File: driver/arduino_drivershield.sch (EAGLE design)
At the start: 22 parts, among them IC1 LB1973M, IC10 LB1973M, IC11 LB1973M, IC12 74HC14D, IC2 LB1973M, IC3 74HC14D, IC4 LB1973M, IC5 LB1973M, IC6 74HC14D, IC7 LB1973M, IC8 LB1973M, IC9 74HC14D, U1 ARDUINO_SHIELDLABEL

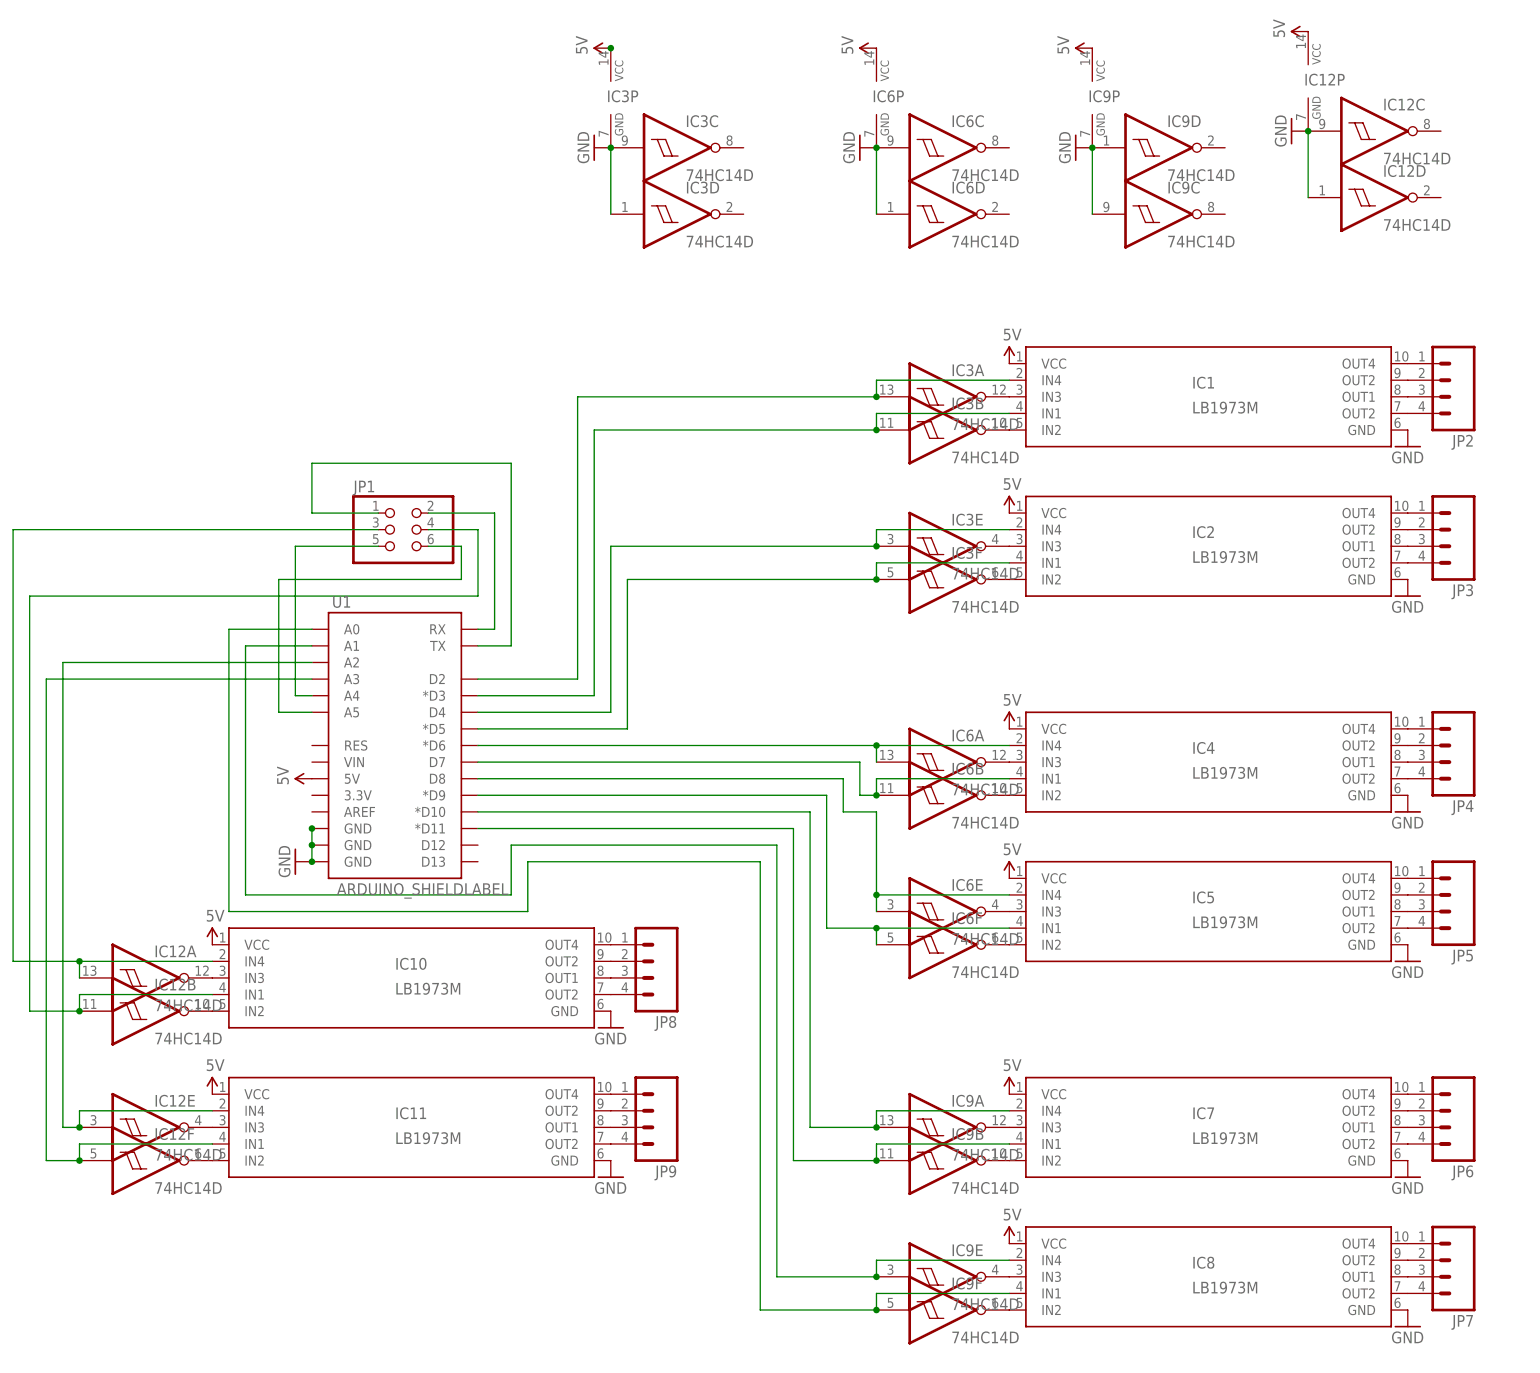
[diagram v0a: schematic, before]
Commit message: attempting to have higher power traces for the h-bridges alone (gnd is a bit tricky if I want to use the plane on the bottom for signal gnd as well
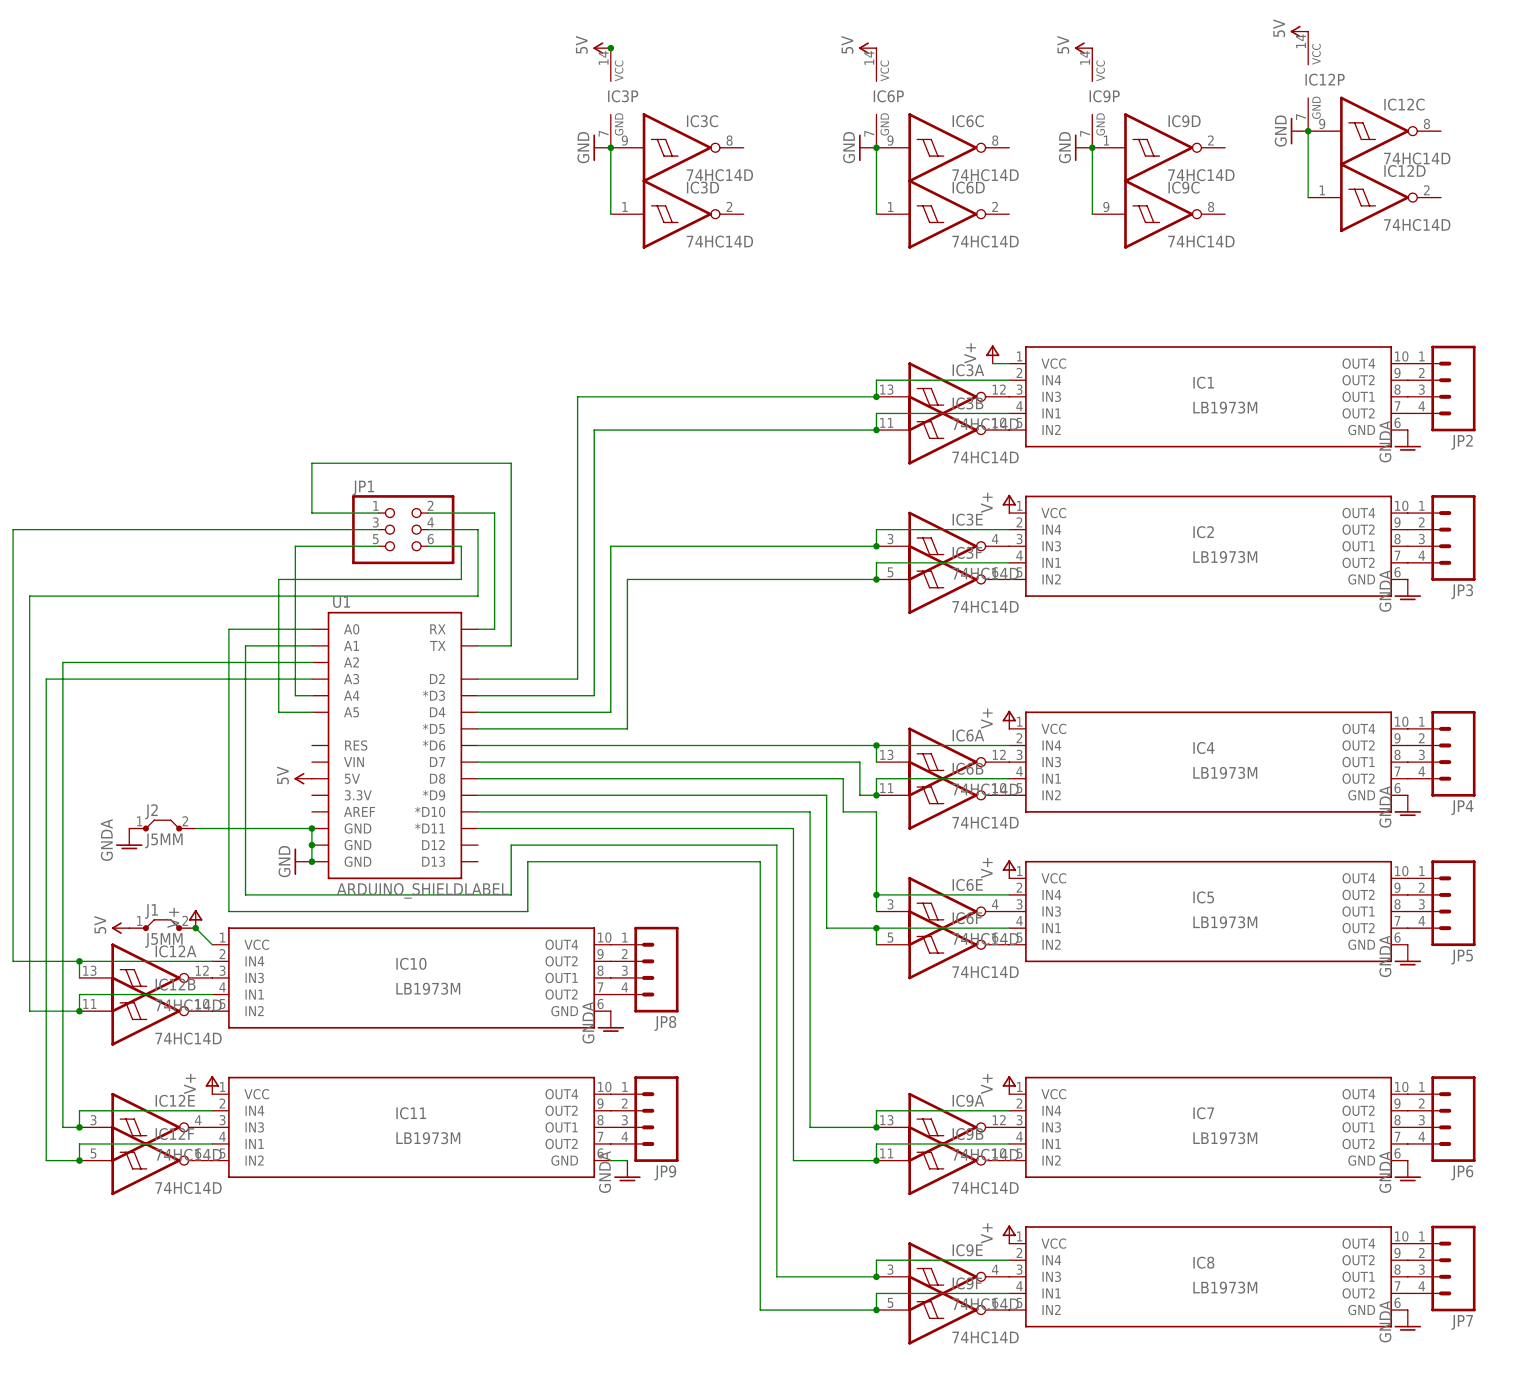
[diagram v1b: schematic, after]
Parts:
- added J1, J2: J5MM, jumper:J5MM
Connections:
- removed net GND: IC1.GND, IC10.GND, IC11.GND, IC12C.I, IC12D.I, IC12P.GND, IC2.GND, IC3C.I, IC3D.I, IC3P.GND, IC4.GND, IC5.GND, IC6C.I, IC6D.I, IC6P.GND, IC7.GND, IC8.GND, IC9C.I, IC9D.I, IC9P.GND, U1.GND@0, U1.GND@1, U1.GND@2
- new net @GND2: IC12C.I, IC12D.I, IC12P.GND, IC3C.I, IC3D.I, IC3P.GND, IC6C.I, IC6D.I, IC6P.GND, IC9C.I, IC9D.I, IC9P.GND, J2.2, U1.GND@0, U1.GND@1, U1.GND@2
- new net @GND3: IC11.GND
- new net GNDA: IC1.GND, IC10.GND, IC2.GND, IC4.GND, IC5.GND, IC7.GND, IC8.GND, J2.1
- new net V+: IC1.VCC, IC10.VCC, IC11.VCC, IC2.VCC, IC4.VCC, IC5.VCC, IC7.VCC, IC8.VCC, J1.2
- net 5V: now also J1.1; no longer IC1.VCC, IC10.VCC, IC11.VCC, IC2.VCC, IC4.VCC, IC5.VCC, IC7.VCC, IC8.VCC

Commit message: bypass caps for all h-bridges
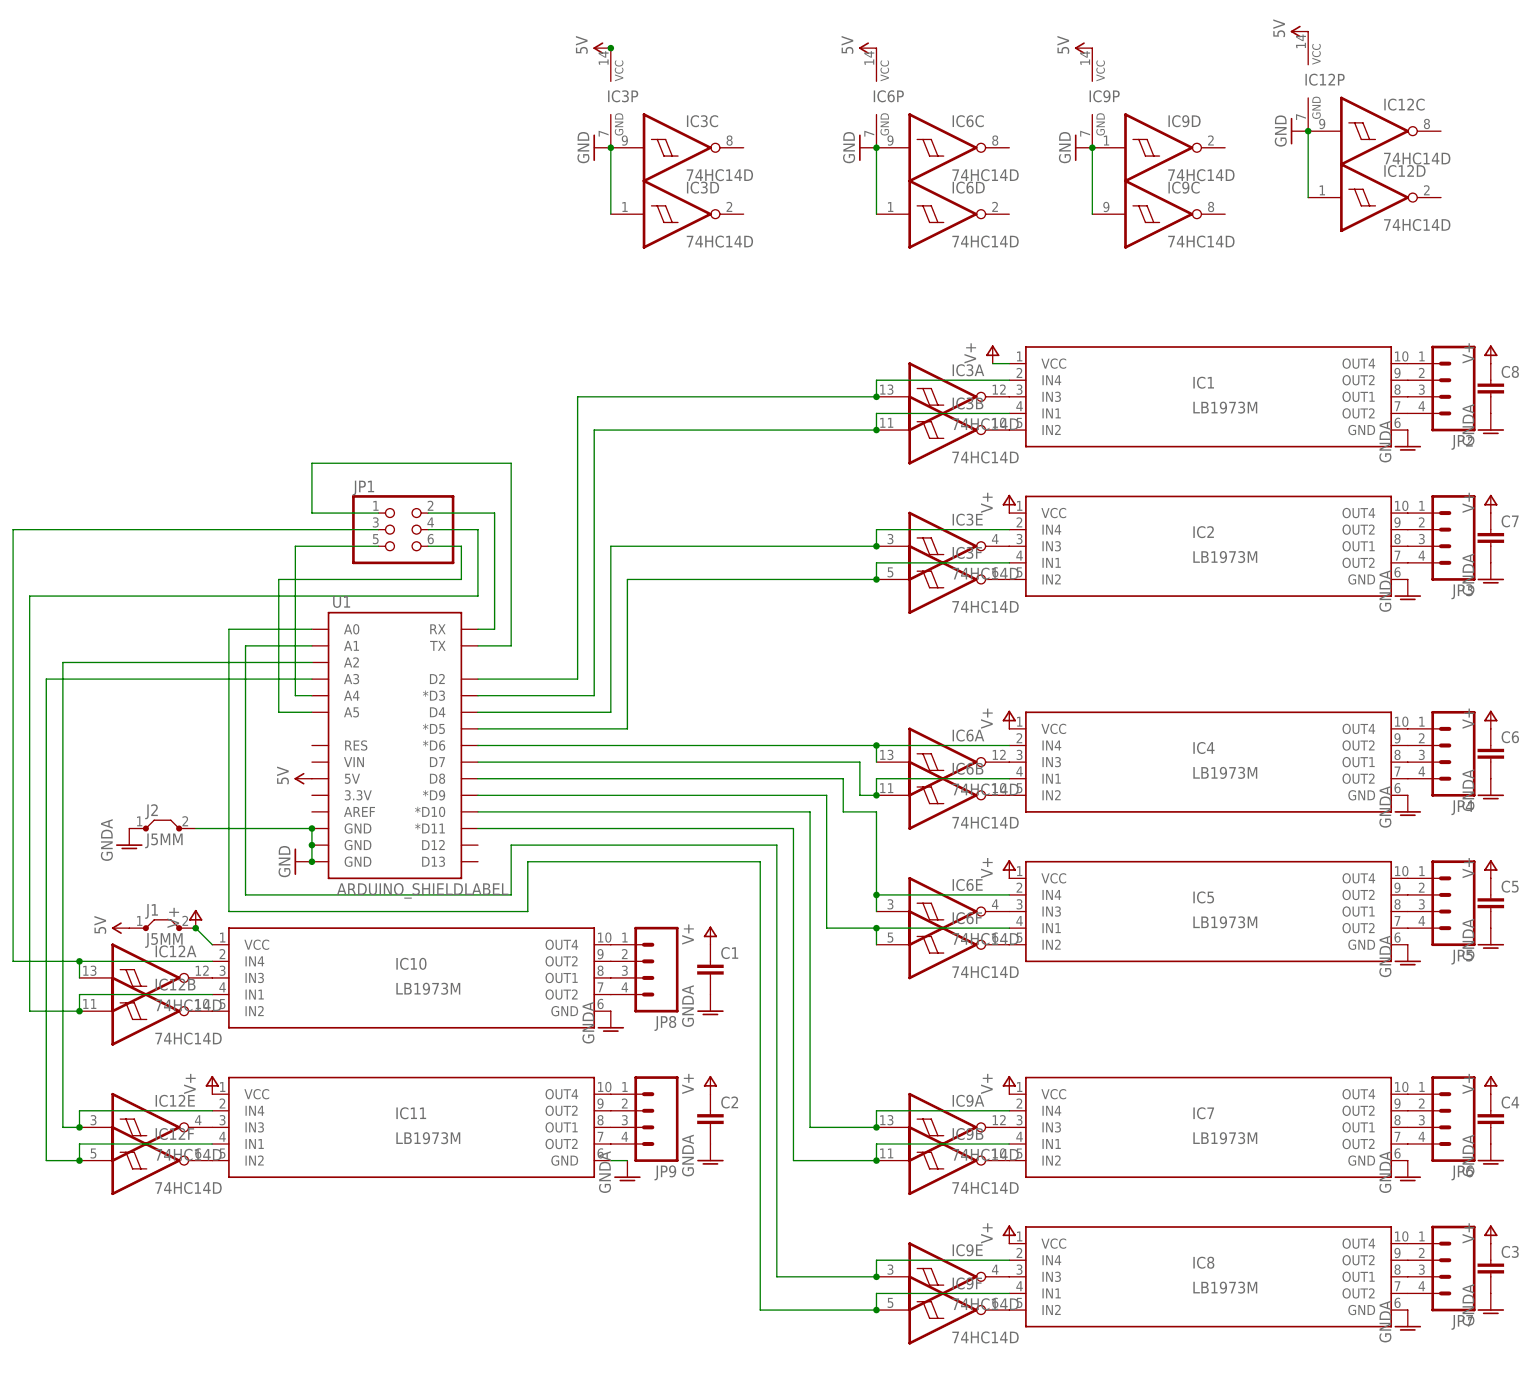
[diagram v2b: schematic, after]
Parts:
- added C1, C2, C3, C4, C5, C6, C7, C8: (no value), rcl:C-EUC0805
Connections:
- net GNDA: now also C1.2, C2.2, C3.2, C4.2, C5.2, C6.2, C7.2, C8.2
- net V+: now also C1.1, C2.1, C3.1, C4.1, C5.1, C6.1, C7.1, C8.1
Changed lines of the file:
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@@
 <part name="J2" library="jumper" deviceset="J" device="5MM"/>
 <part name="GND9" library="supply1" deviceset="GNDA" device=""/>
+<part name="C1" library="rcl" deviceset="C-EU" device="C0805"/>
+<part name="C2" library="rcl" deviceset="C-EU" device="C0805"/>
+<part name="C3" library="rcl" deviceset="C-EU" device="C0805"/>
+<part name="C4" library="rcl" deviceset="C-EU" device="C0805"/>
+<part name="C5" library="rcl" deviceset="C-EU" device="C0805"/>
+<part name="C6" library="rcl" deviceset="C-EU" device="C0805"/>
+<part name="C7" library="rcl" deviceset="C-EU" device="C0805"/>
+<part name="C8" library="rcl" deviceset="C-EU" device="C0805"/>
+<part name="GND15" library="supply1" deviceset="GNDA" device=""/>
+<part name="P+9" library="supply1" deviceset="V+" device=""/>
+<part name="P+10" library="supply1" deviceset="V+" device=""/>
+<part name="GND16" library="supply1" deviceset="GNDA" device=""/>
+<part name="P+11" library="supply1" deviceset="V+" device=""/>
+<part name="GND17" library="supply1" deviceset="GNDA" device=""/>
+<part name="GND18" library="supply1" deviceset="GNDA" device=""/>
+<part name="P+12" library="supply1" deviceset="V+" device=""/>
+<part name="GND19" library="supply1" deviceset="GNDA" device=""/>
+<part name="P+13" library="supply1" deviceset="V+" device=""/>
+<part name="GND20" library="supply1" deviceset="GNDA" device=""/>
+<part name="P+14" library="supply1" deviceset="V+" device=""/>
+<part name="GND21" library="supply1" deviceset="GNDA" device=""/>
+<part name="GND22" library="supply1" deviceset="GNDA" device=""/>
+<part name="P+15" library="supply1" deviceset="V+" device=""/>
+<part name="P+16" library="supply1" deviceset="V+" device=""/>
 </parts>
 <sheets>
@@
 <instance part="J2" gate="1" x="-10.16" y="17.78"/>
 <instance part="GND9" gate="1" x="-15.24" y="15.24"/>
+<instance part="C1" gate="G$1" x="73.66" y="-2.54"/>
+<instance part="C2" gate="G$1" x="73.66" y="-25.4"/>
+<instance part="C3" gate="G$1" x="193.04" y="-48.26"/>
+<instance part="C4" gate="G$1" x="193.04" y="-25.4"/>
+<instance part="C5" gate="G$1" x="193.04" y="7.62"/>
+<instance part="C6" gate="G$1" x="193.04" y="30.48"/>
+<instance part="C7" gate="G$1" x="193.04" y="63.5"/>
+<instance part="C8" gate="G$1" x="193.04" y="86.36"/>
+<instance part="GND15" gate="1" x="193.04" y="78.74"/>
+<instance part="P+9" gate="1" x="193.04" y="91.44"/>
+<instance part="P+10" gate="1" x="193.04" y="68.58"/>
+<instance part="GND16" gate="1" x="193.04" y="55.88"/>
+<instance part="P+11" gate="1" x="193.04" y="35.56"/>
+<instance part="GND17" gate="1" x="193.04" y="22.86"/>
+<instance part="GND18" gate="1" x="193.04" y="0"/>
+<instance part="P+12" gate="1" x="193.04" y="12.7"/>
+<instance part="GND19" gate="1" x="193.04" y="-33.02"/>
+<instance part="P+13" gate="1" x="193.04" y="-20.32"/>
+<instance part="GND20" gate="1" x="193.04" y="-55.88"/>
+<instance part="P+14" gate="1" x="193.04" y="-43.18"/>
+<instance part="GND21" gate="1" x="73.66" y="-33.02"/>
+<instance part="GND22" gate="1" x="73.66" y="-10.16"/>
+<instance part="P+15" gate="1" x="73.66" y="-20.32"/>
+<instance part="P+16" gate="1" x="73.66" y="2.54"/>
 </instances>
 <busses>
@@
 <junction x="-5.08" y="2.54"/>
 </segment>
+<segment>
+<pinref part="C8" gate="G$1" pin="1"/>
+<pinref part="P+9" gate="1" pin="V+"/>
+</segment>
+<segment>
+<pinref part="C7" gate="G$1" pin="1"/>
+<pinref part="P+10" gate="1" pin="V+"/>
+</segment>
+<segment>
+<pinref part="C6" gate="G$1" pin="1"/>
+<pinref part="P+11" gate="1" pin="V+"/>
+</segment>
+<segment>
+<pinref part="C5" gate="G$1" pin="1"/>
+<pinref part="P+12" gate="1" pin="V+"/>
+</segment>
+<segment>
+<pinref part="C4" gate="G$1" pin="1"/>
+<pinref part="P+13" gate="1" pin="V+"/>
+</segment>
+<segment>
+<pinref part="C3" gate="G$1" pin="1"/>
+<pinref part="P+14" gate="1" pin="V+"/>
+</segment>
+<segment>
+<pinref part="C2" gate="G$1" pin="1"/>
+<pinref part="P+15" gate="1" pin="V+"/>
+</segment>
+<segment>
+<pinref part="C1" gate="G$1" pin="1"/>
+<pinref part="P+16" gate="1" pin="V+"/>
+</segment>
 </net>
 <net name="GNDA" class="1">
@@
 <pinref part="GND9" gate="1" pin="GNDA"/>
 </segment>
-</net>
+<segment>
+<pinref part="C8" gate="G$1" pin="2"/>
+<pinref part="GND15" gate="1" pin="GNDA"/>
+</segment>
+<segment>
+<pinref part="C7" gate="G$1" pin="2"/>
+<pinref part="GND16" gate="1" pin="GNDA"/>
+</segment>
+<segment>
+<pinref part="C6" gate="G$1" pin="2"/>
+<pinref part="GND17" gate="1" pin="GNDA"/>
+</segment>
+<segment>
+<pinref part="C5" gate="G$1" pin="2"/>
+<pinref part="GND18" gate="1" pin="GNDA"/>
+</segment>
+<segment>
+<pinref part="C4" gate="G$1" pin="2"/>
+<pinref part="GND19" gate="1" pin="GNDA"/>
+</segment>
+<segment>
+<pinref part="C3" gate="G$1" pin="2"/>
+<pinref part="GND20" gate="1" pin="GNDA"/>
+</segment>
+<segment>
+<pinref part="C2" gate="G$1" pin="2"/>
+<pinref part="GND21" gate="1" pin="GNDA"/>
+</segment>
+<segment>
+<pinref part="C1" gate="G$1" pin="2"/>
+<pinref part="GND22" gate="1" pin="GNDA"/>
+</segment>
+</net>

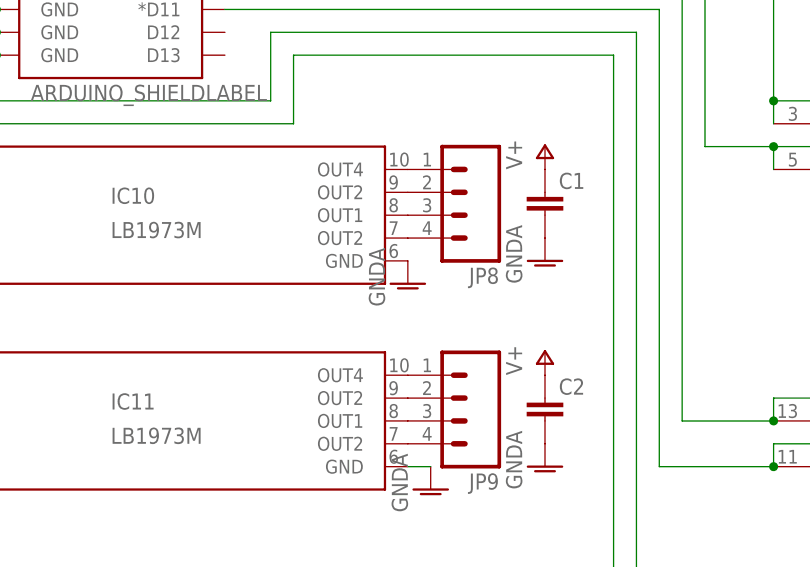
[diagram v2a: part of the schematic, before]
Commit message: the expiriment with the @signal names did not work out
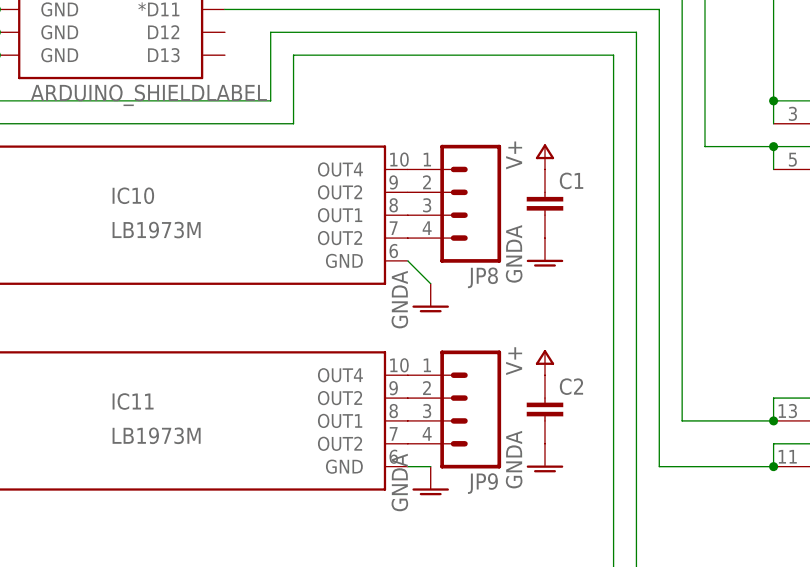
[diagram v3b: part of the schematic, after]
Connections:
- removed net @GND3: IC11.GND
- net GNDA: now also IC11.GND
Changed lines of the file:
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@@
 <instance part="U$3" gate="G$1" x="-15.24" y="2.54" rot="R90"/>
 <instance part="GND14" gate="1" x="60.96" y="-35.56"/>
-<instance part="GND6" gate="1" x="58.42" y="-12.7"/>
+<instance part="GND6" gate="1" x="60.96" y="-15.24"/>
 <instance part="GND7" gate="1" x="180.34" y="-58.42"/>
 <instance part="GND2" gate="1" x="180.34" y="-35.56"/>
@@
 <pinref part="IC10" gate="G$1" pin="GND"/>
 <pinref part="GND6" gate="1" pin="GNDA"/>
+<wire x1="60.96" y1="-12.7" x2="58.42" y2="-10.16" width="0.1524" layer="91"/>
 </segment>
 <segment>
@@
 <pinref part="GND22" gate="1" pin="GNDA"/>
 </segment>
-</net>
-<net name="@GND3" class="1">
 <segment>
 <pinref part="IC11" gate="G$1" pin="GND"/>
